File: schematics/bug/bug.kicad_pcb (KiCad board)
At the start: 2 copper layers, 16 parts, among them P1 CONN_01X09, P2 CONN_01X02, P3 CONN_01X06, P4 CONN_01X02, U1 uln2803A, U2 Arduino_Mini, U3 SPX2920U-3.3, U4 ESP8266, U5 button

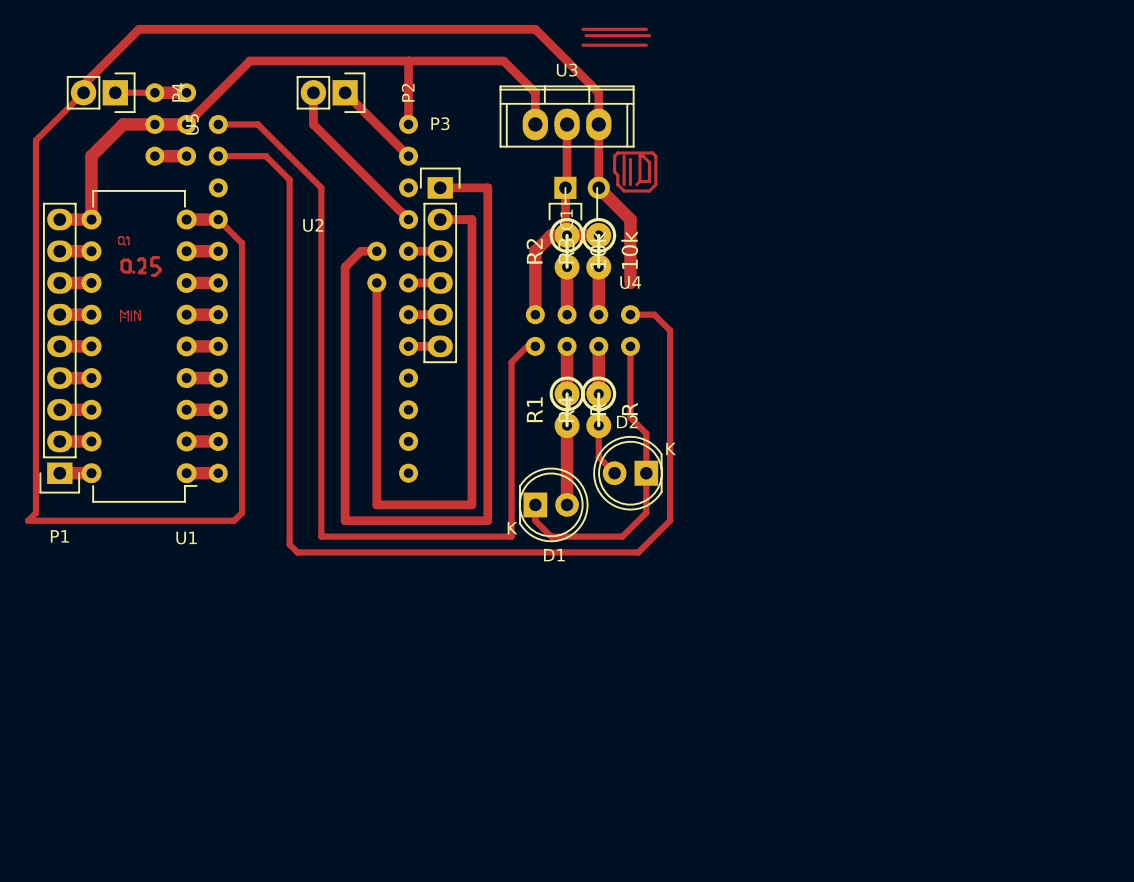
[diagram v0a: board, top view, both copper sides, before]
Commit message: Update schematic lineSensor and bug
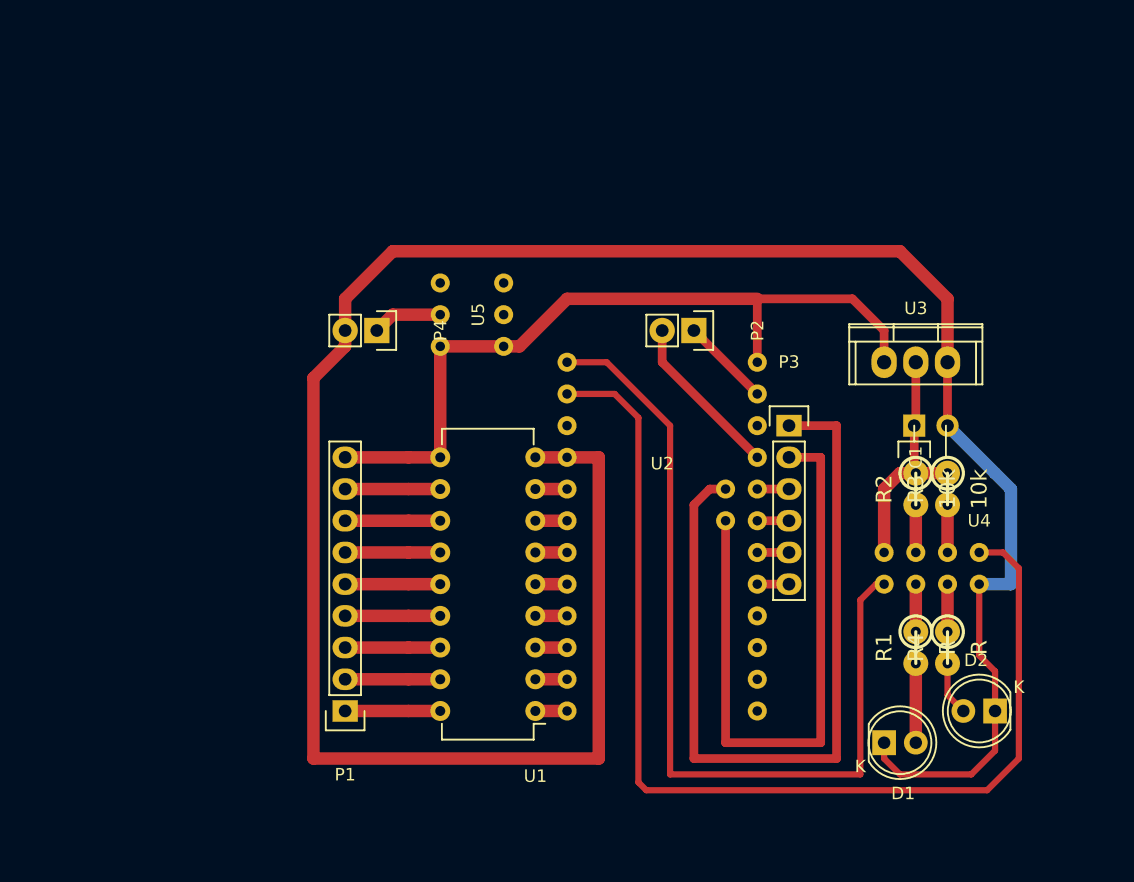
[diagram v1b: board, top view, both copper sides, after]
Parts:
- moved D2 33.8 mm to (171.4, 128.3)
- moved P2 33.8 mm to (147.3, 97.8)
- moved U1 33.8 mm to (134.6, 128.3)
- moved C1 33.8 mm to (167.6, 105.4)
- moved D1 33.8 mm to (162.6, 130.8)
- moved P3 33.8 mm to (154.9, 105.4)
- moved R1 33.8 mm to (165.1, 123.2)
- moved R2 33.8 mm to (165.1, 110.5)
- moved R3 33.8 mm to (167.6, 110.5)
- moved R4 33.8 mm to (167.6, 123.2)
- moved U2 33.8 mm to (144.8, 108.0)
- moved U3 33.8 mm to (165.1, 100.3)
- moved U4 33.8 mm to (167.6, 118.1)
- moved P1 29.8 mm to (119.4, 128.3)
- moved P4 28.3 mm to (121.9, 97.8)
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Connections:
- U5 pad 1: Net-(U5-Pad1) -> Net-(P1-Pad9)
- U5 pad 2: Net-(P1-Pad9) -> Net-(P4-Pad1)
- U5 pad 3: Net-(P4-Pad1) -> Net-(U5-Pad3)
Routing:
- net (no net): track 53.7 -> 0.00 mm
- net Net-(C1-Pad2): track 167.8 -> 194.2 mm
- net Net-(P1-Pad9): track 55.0 -> 62.3 mm
- net Net-(P1-Pad8): track 2.54 -> 7.62 mm
- net Net-(P1-Pad7): track 2.54 -> 7.62 mm
- net Net-(P1-Pad6): track 2.54 -> 7.62 mm
- net Net-(P1-Pad5): track 2.54 -> 7.62 mm
- net Net-(P1-Pad4): track 2.54 -> 7.62 mm
- net Net-(P1-Pad3): track 2.54 -> 7.62 mm
- net Net-(P1-Pad2): track 2.54 -> 7.62 mm
- net Net-(P1-Pad1): track 2.54 -> 7.62 mm
- net Net-(U5-Pad1): track 2.54 -> 0.00 mm

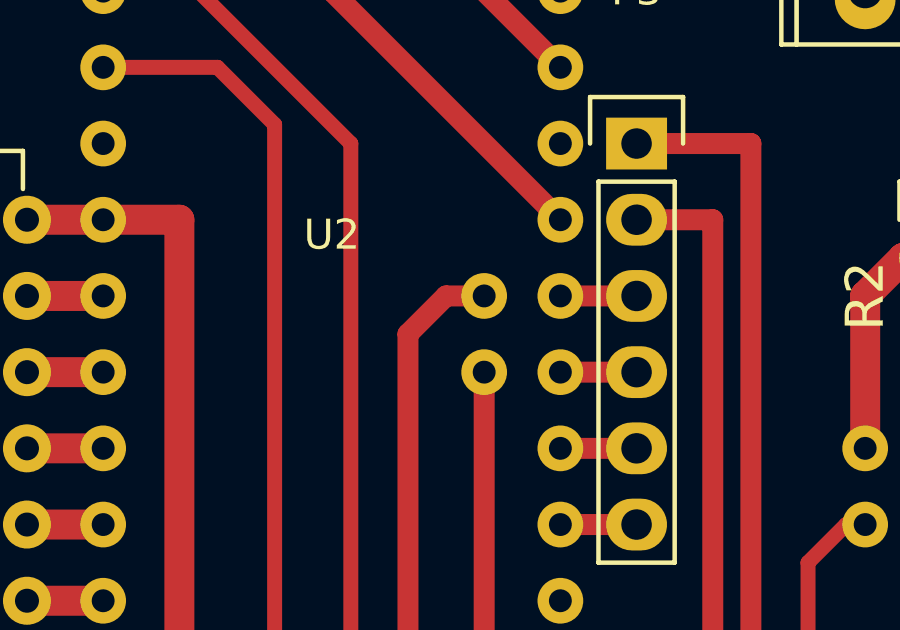
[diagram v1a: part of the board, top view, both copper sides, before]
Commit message: SCHEMATICS: move arduino A4 and A5 pins
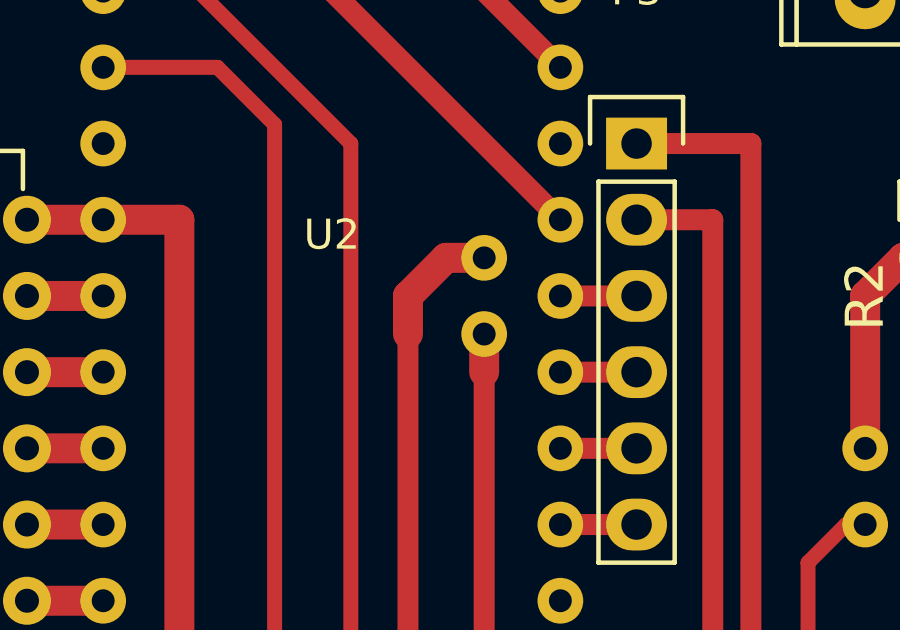
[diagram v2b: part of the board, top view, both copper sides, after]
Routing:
- net Net-(P3-Pad2): track 50.8 -> 52.1 mm
- net Net-(P3-Pad1): track 65.3 -> 66.6 mm
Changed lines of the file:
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@@
     (thickness 1.6)
     (drawings 10)
-    (tracks 110)
+    (tracks 112)
     (zones 0)
     (modules 16)
@@
   )
   (setup
-    (last_trace_width 0.25)
+    (last_trace_width 1)
     (user_trace_width 0.1)
     (user_trace_width 0.5)
@@
     (add_net "Net-(U5-Pad6)")
   )
+  (module bugs:arduino_mini_pro (layer F.Cu)
+    (at 144.78 107.95)
+    (fp_text reference U2 (at 0 0.5) (layer F.SilkS)
+      (effects (font (size 1 1) (thickness 0.15)))
+    )
+    (fp_text value Arduino_Mini (at 0 -0.5) (layer F.Fab)
+      (effects (font (size 1 1) (thickness 0.15)))
+    )
+    (pad 7 thru_hole circle (at 7.62 -7.62) (size 1.524 1.524) (drill 0.762) (layers *.Cu *.Mask F.SilkS)
+      (net 13 "Net-(P1-Pad9)"))
+    (pad 8 thru_hole circle (at 7.62 -5.08) (size 1.524 1.524) (drill 0.762) (layers *.Cu *.Mask F.SilkS)
+      (net 41 "Net-(P2-Pad1)"))
+    (pad 9 thru_hole circle (at 7.62 -2.54) (size 1.524 1.524) (drill 0.762) (layers *.Cu *.Mask F.SilkS)
+      (net 37 "Net-(U2-Pad9)"))
+    (pad 10 thru_hole circle (at 7.62 0) (size 1.524 1.524) (drill 0.762) (layers *.Cu *.Mask F.SilkS)
+      (net 14 "Net-(P2-Pad2)"))
+    (pad 11 thru_hole circle (at 7.62 2.54) (size 1.524 1.524) (drill 0.762) (layers *.Cu *.Mask F.SilkS)
+      (net 17 "Net-(P3-Pad3)"))
+    (pad 12 thru_hole circle (at 7.62 5.08) (size 1.524 1.524) (drill 0.762) (layers *.Cu *.Mask F.SilkS)
+      (net 18 "Net-(P3-Pad4)"))
+    (pad 13 thru_hole circle (at 7.62 7.62) (size 1.524 1.524) (drill 0.762) (layers *.Cu *.Mask F.SilkS)
+      (net 19 "Net-(P3-Pad5)"))
+    (pad 14 thru_hole circle (at 7.62 10.16) (size 1.524 1.524) (drill 0.762) (layers *.Cu *.Mask F.SilkS)
+      (net 20 "Net-(P3-Pad6)"))
+    (pad 15 thru_hole circle (at 7.62 12.7) (size 1.524 1.524) (drill 0.762) (layers *.Cu *.Mask F.SilkS)
+      (net 34 "Net-(U2-Pad15)"))
+    (pad 16 thru_hole circle (at 7.62 15.24) (size 1.524 1.524) (drill 0.762) (layers *.Cu *.Mask F.SilkS)
+      (net 38 "Net-(U2-Pad16)"))
+    (pad 17 thru_hole circle (at 7.62 17.78) (size 1.524 1.524) (drill 0.762) (layers *.Cu *.Mask F.SilkS)
+      (net 39 "Net-(U2-Pad17)"))
+    (pad 18 thru_hole circle (at 7.62 20.32) (size 1.524 1.524) (drill 0.762) (layers *.Cu *.Mask F.SilkS)
+      (net 40 "Net-(U2-Pad18)"))
+    (pad 22 thru_hole circle (at 5.08 1.27) (size 1.524 1.524) (drill 0.762) (layers *.Cu *.Mask F.SilkS)
+      (net 15 "Net-(P3-Pad1)"))
+    (pad 23 thru_hole circle (at 5.08 3.81) (size 1.524 1.524) (drill 0.762) (layers *.Cu *.Mask F.SilkS)
+      (net 16 "Net-(P3-Pad2)"))
+    (pad 24 thru_hole circle (at -7.62 20.32) (size 1.524 1.524) (drill 0.762) (layers *.Cu *.Mask F.SilkS)
+      (net 25 "Net-(U1-Pad1)"))
+    (pad 25 thru_hole circle (at -7.62 17.78) (size 1.524 1.524) (drill 0.762) (layers *.Cu *.Mask F.SilkS)
+      (net 26 "Net-(U1-Pad2)"))
+    (pad 26 thru_hole circle (at -7.62 15.24) (size 1.524 1.524) (drill 0.762) (layers *.Cu *.Mask F.SilkS)
+      (net 27 "Net-(U1-Pad3)"))
+    (pad 27 thru_hole circle (at -7.62 12.7) (size 1.524 1.524) (drill 0.762) (layers *.Cu *.Mask F.SilkS)
+      (net 28 "Net-(U1-Pad4)"))
+    (pad 28 thru_hole circle (at -7.62 10.16) (size 1.524 1.524) (drill 0.762) (layers *.Cu *.Mask F.SilkS)
+      (net 29 "Net-(U1-Pad5)"))
+    (pad 29 thru_hole circle (at -7.62 7.62) (size 1.524 1.524) (drill 0.762) (layers *.Cu *.Mask F.SilkS)
+      (net 30 "Net-(U1-Pad6)"))
+    (pad 30 thru_hole circle (at -7.62 5.08) (size 1.524 1.524) (drill 0.762) (layers *.Cu *.Mask F.SilkS)
+      (net 31 "Net-(U1-Pad7)"))
+    (pad 31 thru_hole circle (at -7.62 2.54) (size 1.524 1.524) (drill 0.762) (layers *.Cu *.Mask F.SilkS)
+      (net 32 "Net-(U1-Pad8)"))
+    (pad 32 thru_hole circle (at -7.62 0) (size 1.524 1.524) (drill 0.762) (layers *.Cu *.Mask F.SilkS)
+      (net 2 "Net-(C1-Pad2)"))
+    (pad 33 thru_hole circle (at -7.62 -2.54) (size 1.524 1.524) (drill 0.762) (layers *.Cu *.Mask F.SilkS)
+      (net 33 "Net-(U2-Pad33)"))
+    (pad 34 thru_hole circle (at -7.62 -5.08) (size 1.524 1.524) (drill 0.762) (layers *.Cu *.Mask F.SilkS)
+      (net 35 "Net-(U2-Pad34)"))
+    (pad 35 thru_hole circle (at -7.62 -7.62) (size 1.524 1.524) (drill 0.762) (layers *.Cu *.Mask F.SilkS)
+      (net 36 "Net-(U2-Pad35)"))
+  )
   (module button (layer F.Cu)
     (at 129.54 96.52 90)
@@
       (rotate (xyz 0 0 0))
     )
-  )
-  (module bugs:arduino_mini_pro (layer F.Cu)
-    (at 144.78 107.95)
-    (fp_text reference U2 (at 0 0.5) (layer F.SilkS)
-      (effects (font (size 1 1) (thickness 0.15)))
-    )
-    (fp_text value Arduino_Mini (at 0 -0.5) (layer F.Fab)
-      (effects (font (size 1 1) (thickness 0.15)))
-    )
-    (pad 7 thru_hole circle (at 7.62 -7.62) (size 1.524 1.524) (drill 0.762) (layers *.Cu *.Mask F.SilkS)
-      (net 13 "Net-(P1-Pad9)"))
-    (pad 8 thru_hole circle (at 7.62 -5.08) (size 1.524 1.524) (drill 0.762) (layers *.Cu *.Mask F.SilkS)
-      (net 41 "Net-(P2-Pad1)"))
-    (pad 9 thru_hole circle (at 7.62 -2.54) (size 1.524 1.524) (drill 0.762) (layers *.Cu *.Mask F.SilkS)
-      (net 37 "Net-(U2-Pad9)"))
-    (pad 10 thru_hole circle (at 7.62 0) (size 1.524 1.524) (drill 0.762) (layers *.Cu *.Mask F.SilkS)
-      (net 14 "Net-(P2-Pad2)"))
-    (pad 11 thru_hole circle (at 7.62 2.54) (size 1.524 1.524) (drill 0.762) (layers *.Cu *.Mask F.SilkS)
-      (net 17 "Net-(P3-Pad3)"))
-    (pad 12 thru_hole circle (at 7.62 5.08) (size 1.524 1.524) (drill 0.762) (layers *.Cu *.Mask F.SilkS)
-      (net 18 "Net-(P3-Pad4)"))
-    (pad 13 thru_hole circle (at 7.62 7.62) (size 1.524 1.524) (drill 0.762) (layers *.Cu *.Mask F.SilkS)
-      (net 19 "Net-(P3-Pad5)"))
-    (pad 14 thru_hole circle (at 7.62 10.16) (size 1.524 1.524) (drill 0.762) (layers *.Cu *.Mask F.SilkS)
-      (net 20 "Net-(P3-Pad6)"))
-    (pad 15 thru_hole circle (at 7.62 12.7) (size 1.524 1.524) (drill 0.762) (layers *.Cu *.Mask F.SilkS)
-      (net 34 "Net-(U2-Pad15)"))
-    (pad 16 thru_hole circle (at 7.62 15.24) (size 1.524 1.524) (drill 0.762) (layers *.Cu *.Mask F.SilkS)
-      (net 38 "Net-(U2-Pad16)"))
-    (pad 17 thru_hole circle (at 7.62 17.78) (size 1.524 1.524) (drill 0.762) (layers *.Cu *.Mask F.SilkS)
-      (net 39 "Net-(U2-Pad17)"))
-    (pad 18 thru_hole circle (at 7.62 20.32) (size 1.524 1.524) (drill 0.762) (layers *.Cu *.Mask F.SilkS)
-      (net 40 "Net-(U2-Pad18)"))
-    (pad 22 thru_hole circle (at 5.08 2.54) (size 1.524 1.524) (drill 0.762) (layers *.Cu *.Mask F.SilkS)
-      (net 15 "Net-(P3-Pad1)"))
-    (pad 23 thru_hole circle (at 5.08 5.08) (size 1.524 1.524) (drill 0.762) (layers *.Cu *.Mask F.SilkS)
-      (net 16 "Net-(P3-Pad2)"))
-    (pad 24 thru_hole circle (at -7.62 20.32) (size 1.524 1.524) (drill 0.762) (layers *.Cu *.Mask F.SilkS)
-      (net 25 "Net-(U1-Pad1)"))
-    (pad 25 thru_hole circle (at -7.62 17.78) (size 1.524 1.524) (drill 0.762) (layers *.Cu *.Mask F.SilkS)
-      (net 26 "Net-(U1-Pad2)"))
-    (pad 26 thru_hole circle (at -7.62 15.24) (size 1.524 1.524) (drill 0.762) (layers *.Cu *.Mask F.SilkS)
-      (net 27 "Net-(U1-Pad3)"))
-    (pad 27 thru_hole circle (at -7.62 12.7) (size 1.524 1.524) (drill 0.762) (layers *.Cu *.Mask F.SilkS)
-      (net 28 "Net-(U1-Pad4)"))
-    (pad 28 thru_hole circle (at -7.62 10.16) (size 1.524 1.524) (drill 0.762) (layers *.Cu *.Mask F.SilkS)
-      (net 29 "Net-(U1-Pad5)"))
-    (pad 29 thru_hole circle (at -7.62 7.62) (size 1.524 1.524) (drill 0.762) (layers *.Cu *.Mask F.SilkS)
-      (net 30 "Net-(U1-Pad6)"))
-    (pad 30 thru_hole circle (at -7.62 5.08) (size 1.524 1.524) (drill 0.762) (layers *.Cu *.Mask F.SilkS)
-      (net 31 "Net-(U1-Pad7)"))
-    (pad 31 thru_hole circle (at -7.62 2.54) (size 1.524 1.524) (drill 0.762) (layers *.Cu *.Mask F.SilkS)
-      (net 32 "Net-(U1-Pad8)"))
-    (pad 32 thru_hole circle (at -7.62 0) (size 1.524 1.524) (drill 0.762) (layers *.Cu *.Mask F.SilkS)
-      (net 2 "Net-(C1-Pad2)"))
-    (pad 33 thru_hole circle (at -7.62 -2.54) (size 1.524 1.524) (drill 0.762) (layers *.Cu *.Mask F.SilkS)
-      (net 33 "Net-(U2-Pad33)"))
-    (pad 34 thru_hole circle (at -7.62 -5.08) (size 1.524 1.524) (drill 0.762) (layers *.Cu *.Mask F.SilkS)
-      (net 35 "Net-(U2-Pad34)"))
-    (pad 35 thru_hole circle (at -7.62 -7.62) (size 1.524 1.524) (drill 0.762) (layers *.Cu *.Mask F.SilkS)
-      (net 36 "Net-(U2-Pad35)"))
   )
   (module Power_Integrations:TO-220 (layer F.Cu)
@@
   (segment (start 144.78 97.79) (end 144.78 100.33) (width 0.7) (layer F.Cu) (net 14))
   (segment (start 144.78 100.33) (end 152.4 107.95) (width 0.7) (layer F.Cu) (net 14))
-  (segment (start 149.86 110.49) (end 148.59 110.49) (width 0.7) (layer F.Cu) (net 15))
+  (segment (start 149.86 109.22) (end 148.59 109.22) (width 1) (layer F.Cu) (net 15) (status 400000))
+  (segment (start 147.32 110.49) (end 147.32 111.76) (width 1) (layer F.Cu) (net 15))
+  (segment (start 148.59 109.22) (end 147.32 110.49) (width 1) (layer F.Cu) (net 15))
   (segment (start 158.75 105.41) (end 154.94 105.41) (width 0.7) (layer F.Cu) (net 15))
   (segment (start 158.75 132.08) (end 158.75 105.41) (width 0.7) (layer F.Cu) (net 15))
   (segment (start 147.32 132.08) (end 158.75 132.08) (width 0.7) (layer F.Cu) (net 15))
   (segment (start 147.32 111.76) (end 147.32 132.08) (width 0.7) (layer F.Cu) (net 15))
-  (segment (start 148.59 110.49) (end 147.32 111.76) (width 0.7) (layer F.Cu) (net 15))
+  (segment (start 149.86 111.76) (end 149.86 113.03) (width 1) (layer F.Cu) (net 16) (status 400000))
   (segment (start 149.86 113.03) (end 149.86 130.81) (width 0.7) (layer F.Cu) (net 16))
   (segment (start 157.48 107.95) (end 154.94 107.95) (width 0.7) (layer F.Cu) (net 16))
